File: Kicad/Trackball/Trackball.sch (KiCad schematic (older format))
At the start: 15 parts, among them J1 52559-1233, J2 Conn_01x04_Male, J3 Conn_01x04_Male, J4 Conn_01x04_Male, J5 Conn_01x04_Male, J6 Conn_01x04_Male, J7 Conn_01x04_Male, J8 Conn_01x04_Male, J9 Conn_01x04_Male, U1 ProMicro

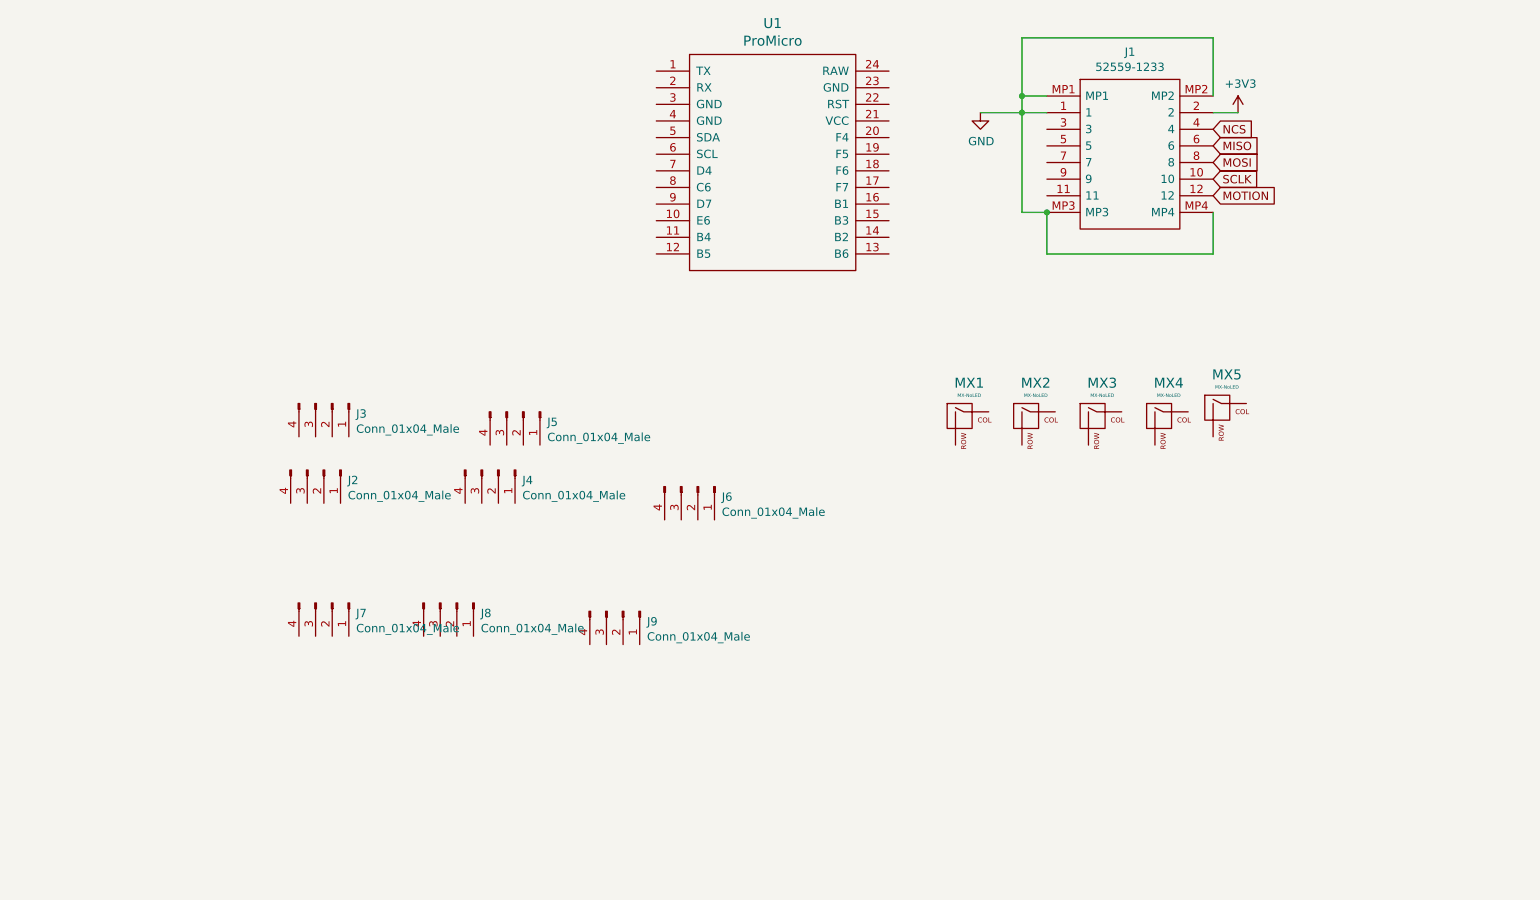
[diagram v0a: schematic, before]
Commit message: Started laying out the schematics and traces.
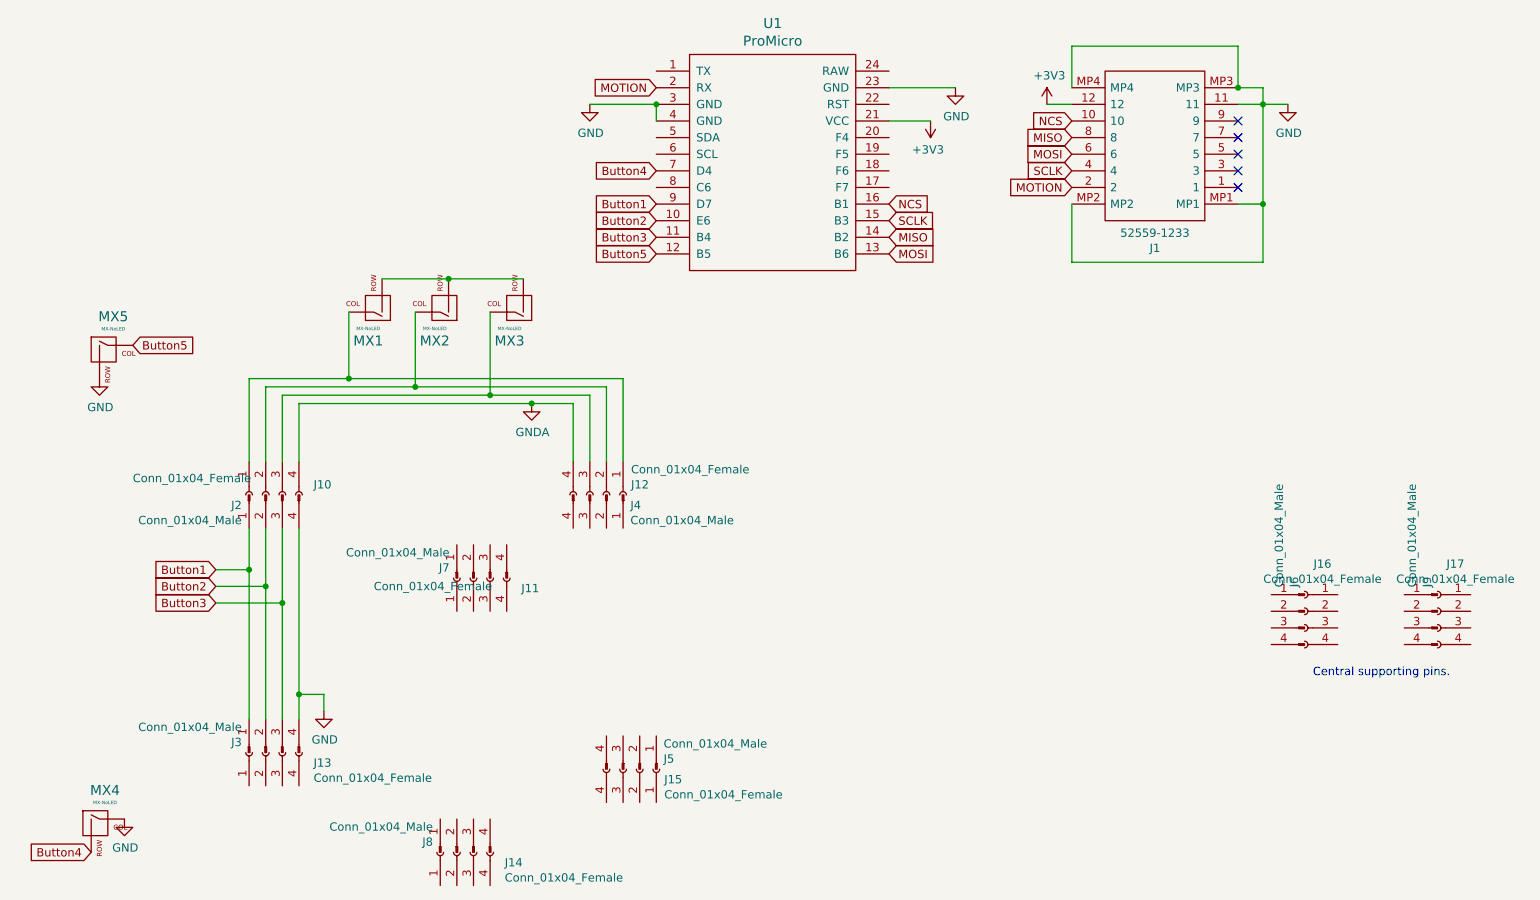
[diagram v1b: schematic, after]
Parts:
- added J10, J11, J12, J13, J14, J15, J16, J17: Conn_01x04_Female, Connector_PinSocket_2.54mm:PinSocket_1x04_P2.54mm_Vertical, symbol Connector:Conn_01x04_Female
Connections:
- net +3V3: now also J1.12, U1.21 (VCC); no longer J1.2
- net GND: now also J1.11, J2.4 (Pin_4), J3.4 (Pin_4), MX4.1 (COL), MX5.2 (ROW), U1.23 (GND), U1.3 (GND), U1.4 (GND); no longer J1.1
- net MISO: now also J1.8, U1.14 (B2); no longer J1.6
- net MOSI: now also J1.6, U1.13 (B6); no longer J1.8
- net MOTION: now also J1.2, U1.2 (RX); no longer J1.12
- net NCS: now also J1.10, U1.16 (B1); no longer J1.4
- net SCLK: now also J1.4, U1.15 (B3); no longer J1.10
- net Button2: now reaches U1.10 (E6)
- net Button2: now also J2.2 (Pin_2), J3.2 (Pin_2)
- net Button3: now reaches U1.11 (B4)
- net Button3: now also J2.3 (Pin_3), J3.3 (Pin_3)
- net Button5: now reaches U1.12 (B5)
- net Button5: now also MX5.1 (COL)
- net Button4: now reaches U1.7 (D4)
- net Button4: now also MX4.2 (ROW)
- net Button1: now reaches U1.9 (D7)
- net Button1: now also J2.1 (Pin_1), J3.1 (Pin_1)
- net at MX1.1 (COL): now also J10.1 (Pin_1), J12.1 (Pin_1)
- net at MX1.2 (ROW): now also MX2.2 (ROW), MX3.2 (ROW)
- net at MX2.1 (COL): now also J10.2 (Pin_2), J12.2 (Pin_2)
- net at MX3.1 (COL): now also J10.3 (Pin_3), J12.3 (Pin_3)
- new net GNDA: J10.4 (Pin_4), J12.4 (Pin_4)
- no-connect marks 0 -> 5
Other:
- note added: "Central supporting pins."
- moved on the sheet: J1, J2, J3, J4, J5, J6, J7, J8, J9, MX1, MX2, MX3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
